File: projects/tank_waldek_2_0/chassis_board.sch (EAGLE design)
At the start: 19 parts, among them U1 NUCLEO-L432KC

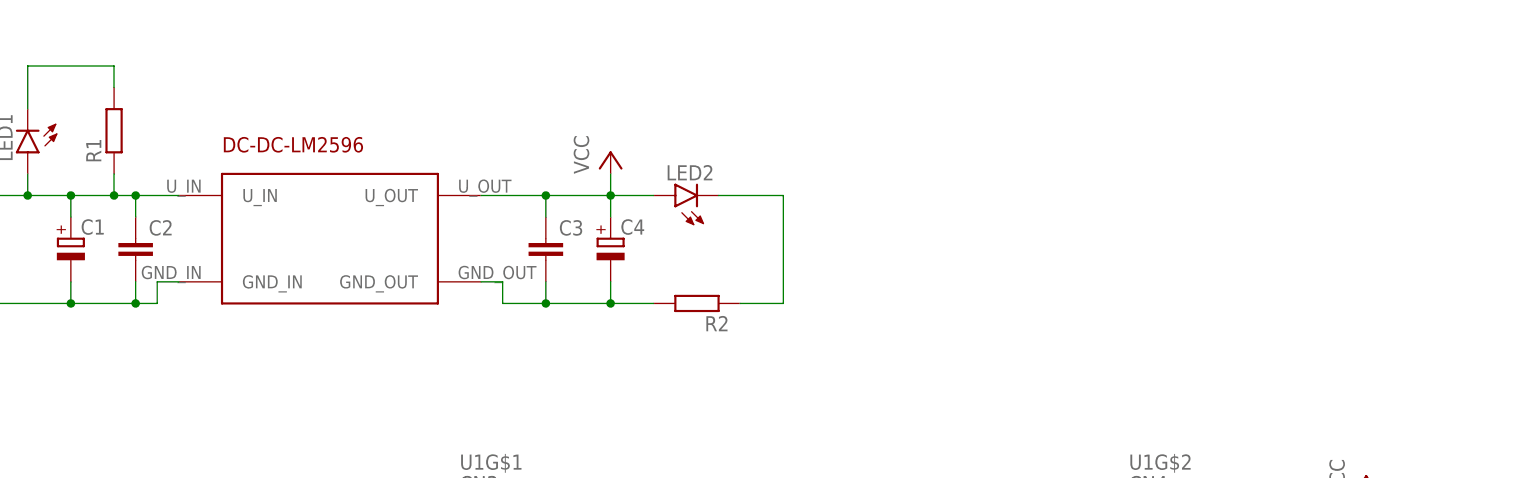
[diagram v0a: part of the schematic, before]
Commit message: miniaturized chassis board
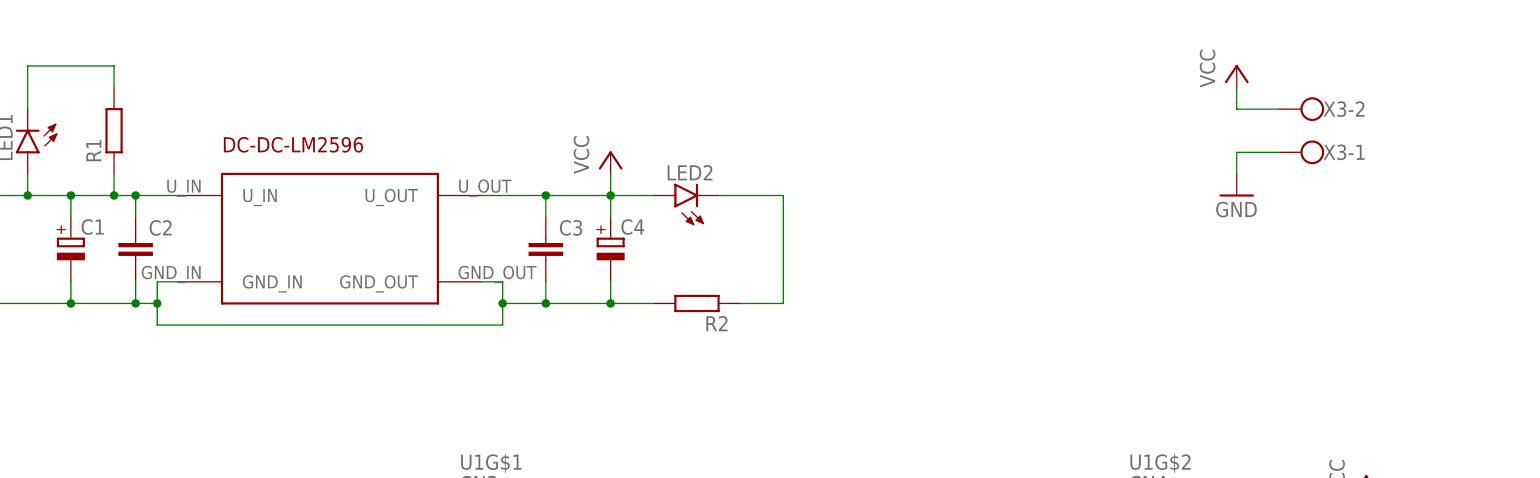
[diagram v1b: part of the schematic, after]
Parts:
- added X3: (no value), con-wago-500:W237-102
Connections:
- removed net N$3: C3.2, C4.-, R2.2, U$6.GND_OUT
- net GND: now also C3.2, C4.-, R2.2, U$6.GND_OUT, X3-1.KL
- net VCC: now also X3-2.KL
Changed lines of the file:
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@@
 <part name="GND4" library="supply1" library_urn="urn:adsk.eagle:library:371" deviceset="GND" device=""/>
 <part name="JP4" library="pinhead" library_urn="urn:adsk.eagle:library:325" deviceset="PINHD-1X4" device="/90" package3d_urn="urn:adsk.eagle:package:22404/2"/>
+<part name="X3" library="con-wago-500" library_urn="urn:adsk.eagle:library:195" deviceset="W237-102" device="" package3d_urn="urn:adsk.eagle:package:10688/1"/>
+<part name="GND5" library="supply1" library_urn="urn:adsk.eagle:library:371" deviceset="GND" device=""/>
+<part name="P+4" library="supply1" library_urn="urn:adsk.eagle:library:371" deviceset="VCC" device=""/>
 </parts>
 <sheets>
@@
 <attribute name="NAME" x="207.01" y="94.615" size="1.778" layer="95"/>
 <attribute name="VALUE" x="207.01" y="78.74" size="1.778" layer="96"/>
+</instance>
+<instance part="X3" gate="-1" x="127" y="83.82" smashed="yes" rot="R180">
+<attribute name="NAME" x="127" y="82.931" size="1.778" layer="95"/>
+</instance>
+<instance part="X3" gate="-2" x="127" y="88.9" smashed="yes" rot="R180">
+<attribute name="VALUE" x="129.54" y="92.583" size="1.778" layer="96" rot="R180"/>
+<attribute name="NAME" x="127" y="88.011" size="1.778" layer="95"/>
+</instance>
+<instance part="GND5" gate="1" x="116.84" y="78.74" smashed="yes">
+<attribute name="VALUE" x="114.3" y="76.2" size="1.778" layer="96"/>
+</instance>
+<instance part="P+4" gate="VCC" x="116.84" y="93.98" smashed="yes">
+<attribute name="VALUE" x="114.3" y="91.44" size="1.778" layer="96" rot="R90"/>
 </instance>
 </instances>
@@
 <wire x1="-12.7" y1="68.58" x2="-12.7" y2="66.04" width="0.1524" layer="91"/>
 <junction x="-12.7" y="66.04"/>
+<wire x1="-10.16" y1="66.04" x2="-10.16" y2="63.5" width="0.1524" layer="91"/>
+<junction x="-10.16" y="66.04"/>
+<wire x1="-10.16" y1="63.5" x2="30.48" y2="63.5" width="0.1524" layer="91"/>
+<pinref part="U$6" gate="G$1" pin="GND_OUT"/>
+<wire x1="27.94" y1="68.58" x2="30.48" y2="68.58" width="0.1524" layer="91"/>
+<wire x1="30.48" y1="68.58" x2="30.48" y2="66.04" width="0.1524" layer="91"/>
+<wire x1="30.48" y1="66.04" x2="35.56" y2="66.04" width="0.1524" layer="91"/>
+<pinref part="C4" gate="G$1" pin="-"/>
+<wire x1="35.56" y1="66.04" x2="43.18" y2="66.04" width="0.1524" layer="91"/>
+<wire x1="43.18" y1="66.04" x2="43.18" y2="68.58" width="0.1524" layer="91"/>
+<pinref part="C3" gate="G$1" pin="2"/>
+<wire x1="35.56" y1="66.04" x2="35.56" y2="68.58" width="0.1524" layer="91"/>
+<junction x="35.56" y="66.04"/>
+<pinref part="R2" gate="G$1" pin="2"/>
+<wire x1="48.26" y1="66.04" x2="43.18" y2="66.04" width="0.1524" layer="91"/>
+<junction x="43.18" y="66.04"/>
+<wire x1="30.48" y1="63.5" x2="30.48" y2="66.04" width="0.1524" layer="91"/>
+<junction x="30.48" y="66.04"/>
 </segment>
 <segment>
@@
 <junction x="198.12" y="88.9"/>
 <pinref part="JP4" gate="A" pin="2"/>
+</segment>
+<segment>
+<pinref part="X3" gate="-1" pin="KL"/>
+<wire x1="121.92" y1="83.82" x2="116.84" y2="83.82" width="0.1524" layer="91"/>
+<pinref part="GND5" gate="1" pin="GND"/>
+<wire x1="116.84" y1="83.82" x2="116.84" y2="81.28" width="0.1524" layer="91"/>
 </segment>
 </net>
@@
 <junction x="198.12" y="91.44"/>
 <pinref part="JP4" gate="A" pin="1"/>
+</segment>
+<segment>
+<pinref part="X3" gate="-2" pin="KL"/>
+<wire x1="121.92" y1="88.9" x2="116.84" y2="88.9" width="0.1524" layer="91"/>
+<pinref part="P+4" gate="VCC" pin="VCC"/>
+<wire x1="116.84" y1="88.9" x2="116.84" y2="91.44" width="0.1524" layer="91"/>
 </segment>
 </net>
@@
 </segment>
 </net>
-<net name="N$3" class="0">
-<segment>
-<pinref part="U$6" gate="G$1" pin="GND_OUT"/>
-<wire x1="27.94" y1="68.58" x2="30.48" y2="68.58" width="0.1524" layer="91"/>
-<wire x1="30.48" y1="68.58" x2="30.48" y2="66.04" width="0.1524" layer="91"/>
-<wire x1="30.48" y1="66.04" x2="35.56" y2="66.04" width="0.1524" layer="91"/>
-<pinref part="C4" gate="G$1" pin="-"/>
-<wire x1="35.56" y1="66.04" x2="43.18" y2="66.04" width="0.1524" layer="91"/>
-<wire x1="43.18" y1="66.04" x2="43.18" y2="68.58" width="0.1524" layer="91"/>
-<pinref part="C3" gate="G$1" pin="2"/>
-<wire x1="35.56" y1="66.04" x2="35.56" y2="68.58" width="0.1524" layer="91"/>
-<junction x="35.56" y="66.04"/>
-<pinref part="R2" gate="G$1" pin="2"/>
-<wire x1="48.26" y1="66.04" x2="43.18" y2="66.04" width="0.1524" layer="91"/>
-<junction x="43.18" y="66.04"/>
-</segment>
-</net>

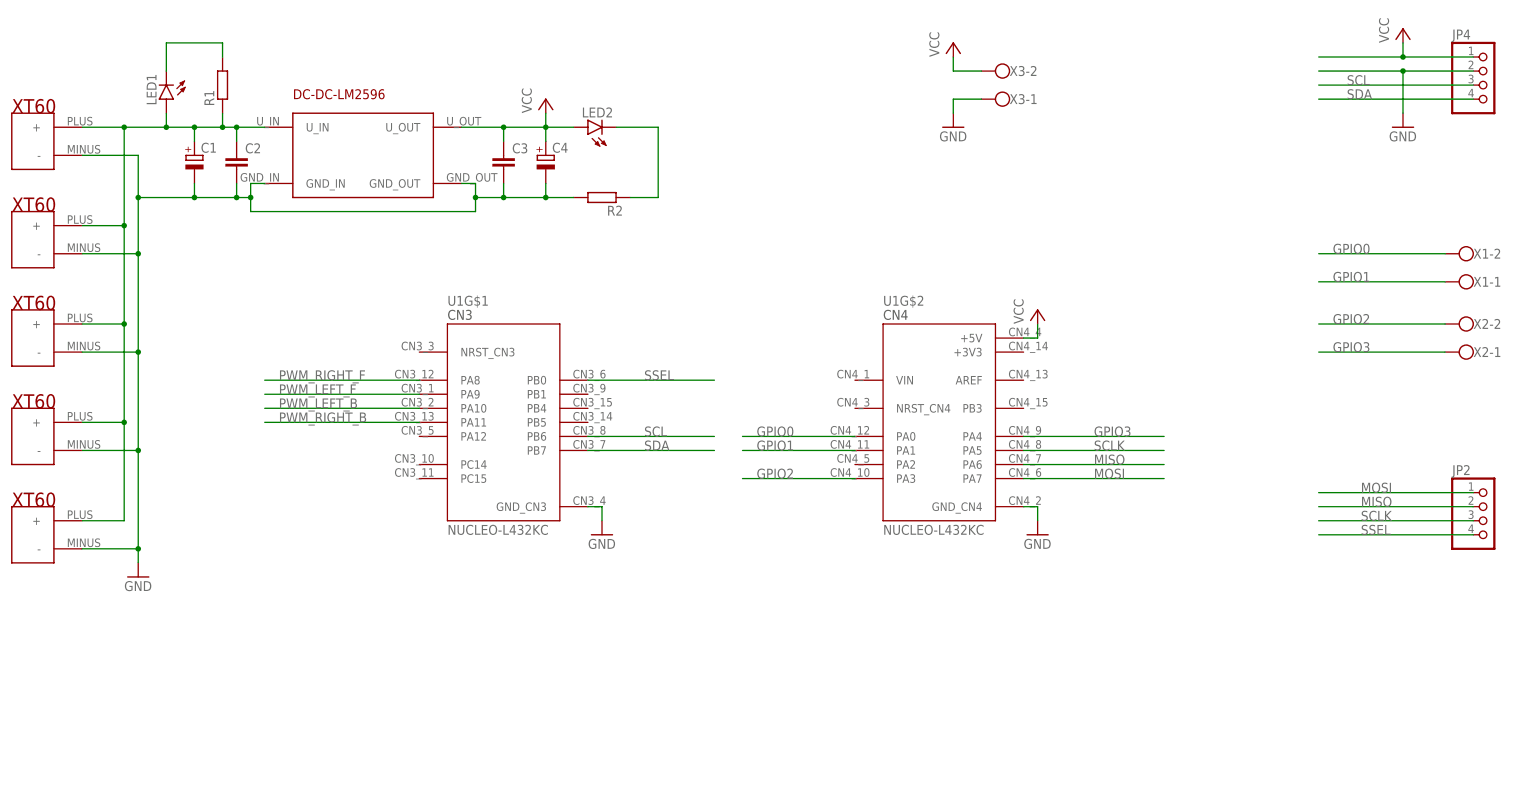
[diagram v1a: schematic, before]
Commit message: fixed waldek missing pwm outputs, wop on gramofon
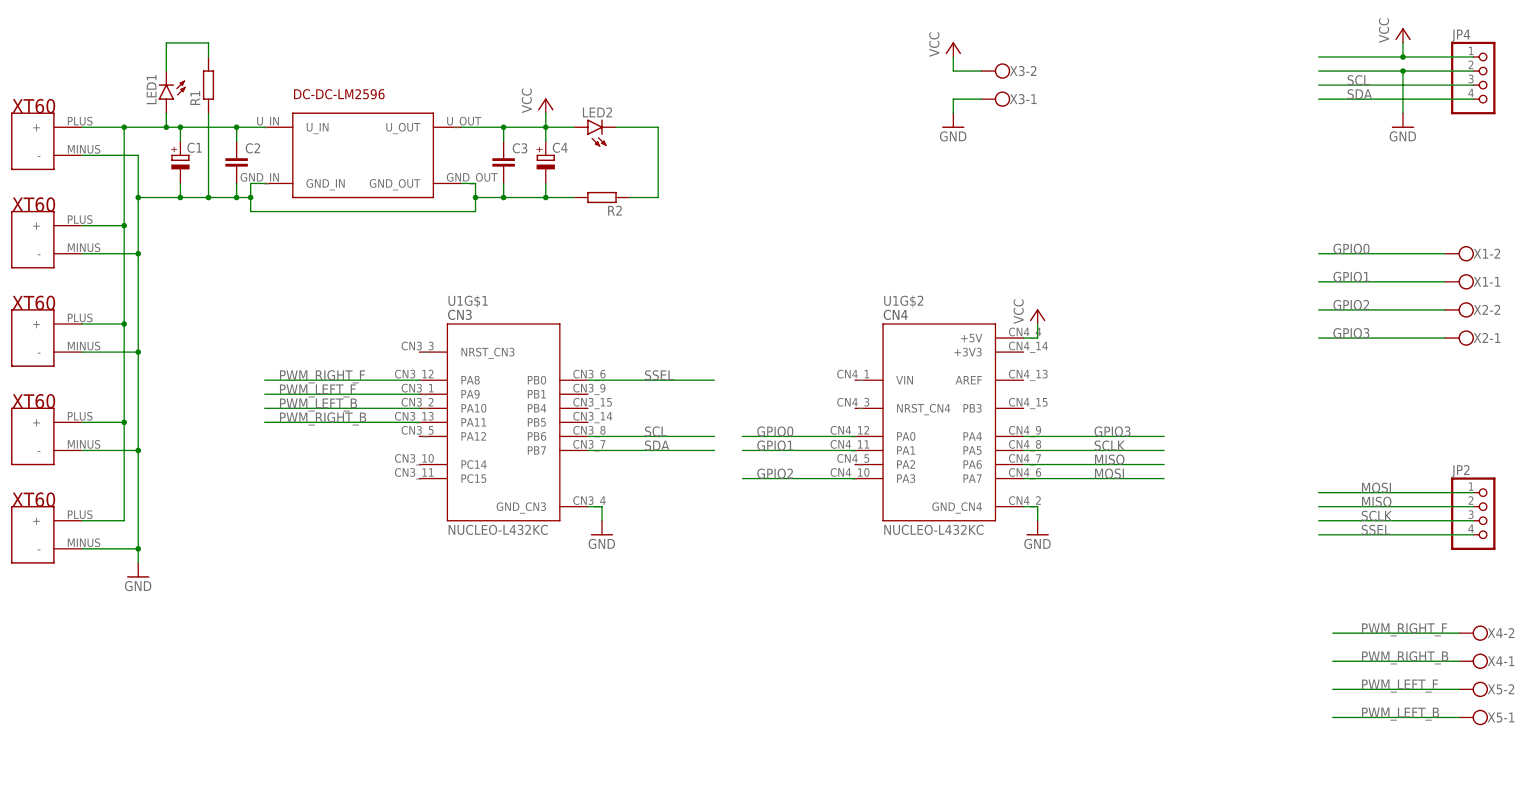
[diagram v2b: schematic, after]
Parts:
- added X4, X5: (no value), con-wago-500:W237-102
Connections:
- net GND: now also R1.1
- net N$1: no longer R1.1
- net PWM_LEFT_B: now also X5-1.KL
- net PWM_LEFT_F: now also X5-2.KL
- net PWM_RIGHT_B: now also X4-1.KL
- net PWM_RIGHT_F: now also X4-2.KL
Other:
- moved on the sheet: C1, R1, X2-1, X2-2
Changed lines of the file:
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@@
 <part name="GND5" library="supply1" library_urn="urn:adsk.eagle:library:371" deviceset="GND" device=""/>
 <part name="P+4" library="supply1" library_urn="urn:adsk.eagle:library:371" deviceset="VCC" device=""/>
+<part name="X4" library="con-wago-500" library_urn="urn:adsk.eagle:library:195" deviceset="W237-102" device="" package3d_urn="urn:adsk.eagle:package:10688/1"/>
+<part name="X5" library="con-wago-500" library_urn="urn:adsk.eagle:library:195" deviceset="W237-102" device="" package3d_urn="urn:adsk.eagle:package:10688/1"/>
 </parts>
 <sheets>
@@
 <attribute name="VALUE" x="37.084" y="68.961" size="1.778" layer="96"/>
 </instance>
-<instance part="C1" gate="G$1" x="-20.32" y="73.66" smashed="yes">
-<attribute name="NAME" x="-19.177" y="74.1426" size="1.778" layer="95"/>
-<attribute name="VALUE" x="-19.177" y="69.0626" size="1.778" layer="96"/>
+<instance part="C1" gate="G$1" x="-22.86" y="73.66" smashed="yes">
+<attribute name="NAME" x="-21.717" y="74.1426" size="1.778" layer="95"/>
+<attribute name="VALUE" x="-21.717" y="69.0626" size="1.778" layer="96"/>
 </instance>
 <instance part="C4" gate="G$1" x="43.18" y="73.66" smashed="yes">
@@
 <attribute name="VALUE" x="-31.115" y="88.392" size="1.778" layer="96" rot="R270"/>
 </instance>
-<instance part="R1" gate="G$1" x="-15.24" y="86.36" smashed="yes" rot="R90">
-<attribute name="NAME" x="-16.7386" y="82.55" size="1.778" layer="95" rot="R90"/>
-<attribute name="VALUE" x="-11.938" y="82.55" size="1.778" layer="96" rot="R90"/>
+<instance part="R1" gate="G$1" x="-17.78" y="86.36" smashed="yes" rot="R90">
+<attribute name="NAME" x="-19.2786" y="82.55" size="1.778" layer="95" rot="R90"/>
+<attribute name="VALUE" x="-14.478" y="82.55" size="1.778" layer="96" rot="R90"/>
 </instance>
 <instance part="R2" gate="G$1" x="53.34" y="66.04" smashed="yes" rot="R180">
@@
 <attribute name="NAME" x="210.82" y="54.991" size="1.778" layer="95"/>
 </instance>
-<instance part="X2" gate="-1" x="210.82" y="38.1" smashed="yes" rot="R180">
-<attribute name="NAME" x="210.82" y="37.211" size="1.778" layer="95"/>
-</instance>
-<instance part="X2" gate="-2" x="210.82" y="43.18" smashed="yes" rot="R180">
-<attribute name="VALUE" x="213.36" y="46.863" size="1.778" layer="96" rot="R180"/>
-<attribute name="NAME" x="210.82" y="42.291" size="1.778" layer="95"/>
+<instance part="X2" gate="-1" x="210.82" y="40.64" smashed="yes" rot="R180">
+<attribute name="NAME" x="210.82" y="39.751" size="1.778" layer="95"/>
+</instance>
+<instance part="X2" gate="-2" x="210.82" y="45.72" smashed="yes" rot="R180">
+<attribute name="VALUE" x="213.36" y="49.403" size="1.778" layer="96" rot="R180"/>
+<attribute name="NAME" x="210.82" y="44.831" size="1.778" layer="95"/>
 </instance>
 <instance part="JP2" gate="A" x="213.36" y="7.62" smashed="yes">
@@
 <instance part="P+4" gate="VCC" x="116.84" y="93.98" smashed="yes">
 <attribute name="VALUE" x="114.3" y="91.44" size="1.778" layer="96" rot="R90"/>
+</instance>
+<instance part="X4" gate="-1" x="213.36" y="-17.78" smashed="yes" rot="R180">
+<attribute name="NAME" x="213.36" y="-18.669" size="1.778" layer="95"/>
+</instance>
+<instance part="X4" gate="-2" x="213.36" y="-12.7" smashed="yes" rot="R180">
+<attribute name="VALUE" x="215.9" y="-9.017" size="1.778" layer="96" rot="R180"/>
+<attribute name="NAME" x="213.36" y="-13.589" size="1.778" layer="95"/>
+</instance>
+<instance part="X5" gate="-1" x="213.36" y="-27.94" smashed="yes" rot="R180">
+<attribute name="NAME" x="213.36" y="-28.829" size="1.778" layer="95"/>
+</instance>
+<instance part="X5" gate="-2" x="213.36" y="-22.86" smashed="yes" rot="R180">
+<attribute name="VALUE" x="215.9" y="-19.177" size="1.778" layer="96" rot="R180"/>
+<attribute name="NAME" x="213.36" y="-23.749" size="1.778" layer="95"/>
 </instance>
 </instances>
@@
 <junction x="-30.48" y="66.04"/>
 <pinref part="C1" gate="G$1" pin="-"/>
-<wire x1="-12.7" y1="66.04" x2="-20.32" y2="66.04" width="0.1524" layer="91"/>
-<wire x1="-20.32" y1="66.04" x2="-30.48" y2="66.04" width="0.1524" layer="91"/>
-<wire x1="-20.32" y1="68.58" x2="-20.32" y2="66.04" width="0.1524" layer="91"/>
-<junction x="-20.32" y="66.04"/>
+<wire x1="-12.7" y1="66.04" x2="-17.78" y2="66.04" width="0.1524" layer="91"/>
+<wire x1="-17.78" y1="66.04" x2="-22.86" y2="66.04" width="0.1524" layer="91"/>
+<wire x1="-22.86" y1="66.04" x2="-30.48" y2="66.04" width="0.1524" layer="91"/>
+<wire x1="-22.86" y1="68.58" x2="-22.86" y2="66.04" width="0.1524" layer="91"/>
+<junction x="-22.86" y="66.04"/>
 <pinref part="C2" gate="G$1" pin="2"/>
 <wire x1="-12.7" y1="68.58" x2="-12.7" y2="66.04" width="0.1524" layer="91"/>
@@
 <wire x1="30.48" y1="63.5" x2="30.48" y2="66.04" width="0.1524" layer="91"/>
 <junction x="30.48" y="66.04"/>
+<pinref part="R1" gate="G$1" pin="1"/>
+<wire x1="-17.78" y1="81.28" x2="-17.78" y2="66.04" width="0.1524" layer="91"/>
+<junction x="-17.78" y="66.04"/>
 </segment>
 <segment>
@@
 <wire x1="-33.02" y1="78.74" x2="-25.4" y2="78.74" width="0.1524" layer="91"/>
 <pinref part="C2" gate="G$1" pin="1"/>
-<wire x1="-25.4" y1="78.74" x2="-20.32" y2="78.74" width="0.1524" layer="91"/>
-<wire x1="-20.32" y1="78.74" x2="-15.24" y2="78.74" width="0.1524" layer="91"/>
-<wire x1="-15.24" y1="78.74" x2="-12.7" y2="78.74" width="0.1524" layer="91"/>
+<wire x1="-25.4" y1="78.74" x2="-22.86" y2="78.74" width="0.1524" layer="91"/>
+<wire x1="-22.86" y1="78.74" x2="-12.7" y2="78.74" width="0.1524" layer="91"/>
 <wire x1="-12.7" y1="78.74" x2="-7.62" y2="78.74" width="0.1524" layer="91"/>
 <wire x1="-12.7" y1="76.2" x2="-12.7" y2="78.74" width="0.1524" layer="91"/>
 <junction x="-12.7" y="78.74"/>
 <pinref part="C1" gate="G$1" pin="+"/>
-<wire x1="-20.32" y1="76.2" x2="-20.32" y2="78.74" width="0.1524" layer="91"/>
-<junction x="-20.32" y="78.74"/>
-<pinref part="R1" gate="G$1" pin="1"/>
-<wire x1="-15.24" y1="78.74" x2="-15.24" y2="81.28" width="0.1524" layer="91"/>
-<junction x="-15.24" y="78.74"/>
+<wire x1="-22.86" y1="76.2" x2="-22.86" y2="78.74" width="0.1524" layer="91"/>
+<junction x="-22.86" y="78.74"/>
 <pinref part="LED1" gate="G$1" pin="A"/>
 <wire x1="-25.4" y1="81.28" x2="-25.4" y2="78.74" width="0.1524" layer="91"/>
@@
 <pinref part="LED1" gate="G$1" pin="C"/>
 <wire x1="-25.4" y1="88.9" x2="-25.4" y2="93.98" width="0.1524" layer="91"/>
-<wire x1="-25.4" y1="93.98" x2="-15.24" y2="93.98" width="0.1524" layer="91"/>
+<wire x1="-25.4" y1="93.98" x2="-17.78" y2="93.98" width="0.1524" layer="91"/>
 <pinref part="R1" gate="G$1" pin="2"/>
-<wire x1="-15.24" y1="93.98" x2="-15.24" y2="91.44" width="0.1524" layer="91"/>
+<wire x1="-17.78" y1="93.98" x2="-17.78" y2="91.44" width="0.1524" layer="91"/>
 </segment>
 </net>
@@
 <segment>
 <pinref part="X2" gate="-2" pin="KL"/>
-<wire x1="205.74" y1="43.18" x2="182.88" y2="43.18" width="0.1524" layer="91"/>
-<label x="185.42" y="43.18" size="1.778" layer="95"/>
+<wire x1="205.74" y1="45.72" x2="182.88" y2="45.72" width="0.1524" layer="91"/>
+<label x="185.42" y="45.72" size="1.778" layer="95"/>
 </segment>
 <segment>
@@
 <segment>
 <pinref part="X2" gate="-1" pin="KL"/>
-<wire x1="205.74" y1="38.1" x2="182.88" y2="38.1" width="0.1524" layer="91"/>
-<label x="185.42" y="38.1" size="1.778" layer="95"/>
+<wire x1="205.74" y1="40.64" x2="182.88" y2="40.64" width="0.1524" layer="91"/>
+<label x="185.42" y="40.64" size="1.778" layer="95"/>
 </segment>
 <segment>
@@
 <label x="-5.08" y="30.48" size="1.778" layer="95"/>
 </segment>
+<segment>
+<pinref part="X5" gate="-2" pin="KL"/>
+<wire x1="208.28" y1="-22.86" x2="185.42" y2="-22.86" width="0.1524" layer="91"/>
+<label x="190.5" y="-22.86" size="1.778" layer="95"/>
+</segment>
 </net>
 <net name="PWM_LEFT_B" class="0">
@@
 <label x="-5.08" y="27.94" size="1.778" layer="95"/>
 </segment>
+<segment>
+<pinref part="X5" gate="-1" pin="KL"/>
+<wire x1="208.28" y1="-27.94" x2="185.42" y2="-27.94" width="0.1524" layer="91"/>
+<label x="190.5" y="-27.94" size="1.778" layer="95"/>
+</segment>
 </net>
 <net name="PWM_RIGHT_F" class="0">
@@
 <label x="-5.08" y="33.02" size="1.778" layer="95"/>
 </segment>
+<segment>
+<pinref part="X4" gate="-2" pin="KL"/>
+<wire x1="208.28" y1="-12.7" x2="185.42" y2="-12.7" width="0.1524" layer="91"/>
+<label x="190.5" y="-12.7" size="1.778" layer="95"/>
+</segment>
 </net>
 <net name="PWM_RIGHT_B" class="0">
@@
 <label x="-5.08" y="25.4" size="1.778" layer="95"/>
 </segment>
-</net>
+<segment>
+<pinref part="X4" gate="-1" pin="KL"/>
+<wire x1="208.28" y1="-17.78" x2="185.42" y2="-17.78" width="0.1524" layer="91"/>
+<label x="190.5" y="-17.78" size="1.778" layer="95"/>
+</segment>
+</net>
